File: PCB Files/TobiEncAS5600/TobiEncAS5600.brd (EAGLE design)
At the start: 16 x 16 mm, 4 parts

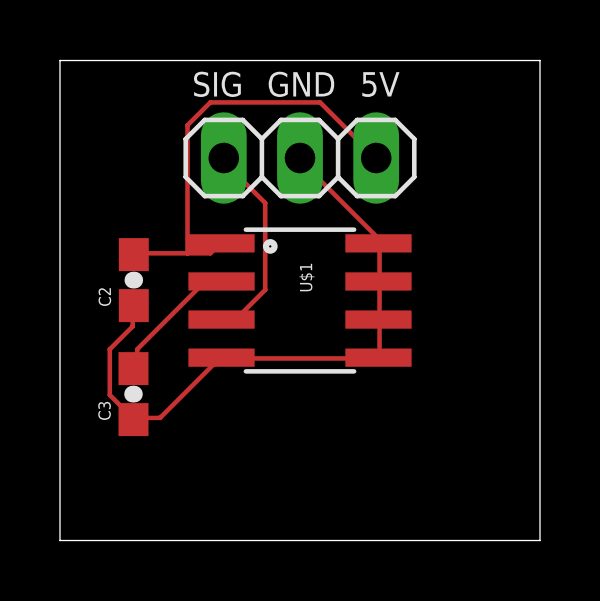
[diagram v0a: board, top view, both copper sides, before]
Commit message: heavier traces on encoder board since it can accomodate them
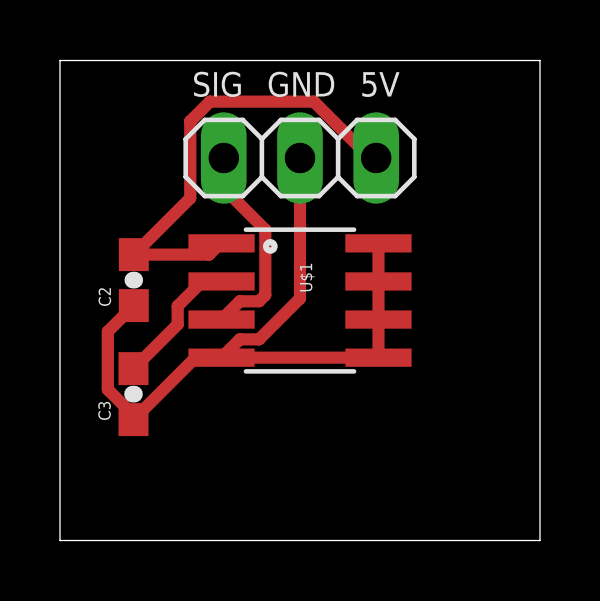
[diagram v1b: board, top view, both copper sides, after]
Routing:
- net GND: track 21.3 -> 25.5 mm
- net 5V: track 14.7 -> 15.7 mm
- net VDD3V3: track 4.51 -> 5.38 mm
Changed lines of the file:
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@@
 <contactref element="C2" pad="2"/>
 <contactref element="JP1" pad="1"/>
-<wire x1="23.0124" y1="93.5736" x2="22.2504" y2="93.5736" width="0.1524" layer="1"/>
-<wire x1="22.2504" y1="93.5736" x2="20.574" y2="93.5736" width="0.1524" layer="1"/>
-<wire x1="23.3172" y1="93.8784" x2="23.0124" y2="93.5736" width="0.1524" layer="1"/>
 <wire x1="20.574" y1="93.5736" x2="20.46" y2="93.53" width="0.1524" layer="1"/>
 <wire x1="23.3172" y1="93.8784" x2="23.3838" y2="93.905" width="0.1524" layer="1"/>
-<wire x1="22.2504" y1="97.8408" x2="22.2504" y2="93.5736" width="0.1524" layer="1"/>
-<wire x1="23.0124" y1="98.6028" x2="22.2504" y2="97.8408" width="0.1524" layer="1"/>
-<wire x1="26.67" y1="98.6028" x2="23.0124" y2="98.6028" width="0.1524" layer="1"/>
-<wire x1="28.4988" y1="96.774" x2="26.67" y2="98.6028" width="0.1524" layer="1"/>
-<wire x1="28.4988" y1="96.774" x2="28.54" y2="96.75" width="0.1524" layer="1"/>
+<wire x1="20.46" y1="93.53" x2="22.9688" y2="93.53" width="0.4064" layer="1"/>
+<wire x1="22.9688" y1="93.53" x2="23.3172" y2="93.8784" width="0.4064" layer="1"/>
+<wire x1="22.99706875" y1="98.6296" x2="22.3424" y2="97.97493125" width="0.4064" layer="1"/>
+<wire x1="28.54" y1="96.75" x2="28.34253125" y2="96.75" width="0.4064" layer="1"/>
+<wire x1="22.3424" y1="95.4124" x2="20.46" y2="93.53" width="0.4064" layer="1"/>
+<wire x1="28.34253125" y1="96.75" x2="26.46293125" y2="98.6296" width="0.4064" layer="1"/>
+<wire x1="22.3424" y1="97.97493125" x2="22.3424" y2="95.4124" width="0.4064" layer="1"/>
+<wire x1="26.46293125" y1="98.6296" x2="22.99706875" y2="98.6296" width="0.4064" layer="1"/>
 </signal>
 <signal name="SIG">
 <contactref element="U$1" pad="3"/>
 <contactref element="JP1" pad="3"/>
-<wire x1="23.9268" y1="91.44" x2="23.4696" y2="91.44" width="0.1524" layer="1"/>
-<wire x1="24.8412" y1="92.3544" x2="23.9268" y2="91.44" width="0.1524" layer="1"/>
-<wire x1="24.8412" y1="95.25" x2="24.8412" y2="92.3544" width="0.1524" layer="1"/>
-<wire x1="23.4696" y1="96.6216" x2="24.8412" y2="95.25" width="0.1524" layer="1"/>
-<wire x1="23.4696" y1="91.44" x2="23.3838" y2="91.365" width="0.1524" layer="1"/>
-<wire x1="23.4696" y1="96.6216" x2="23.46" y2="96.75" width="0.1524" layer="1"/>
+<wire x1="24.63599375" y1="91.9746" x2="24.8443" y2="92.18290625" width="0.4064" layer="1"/>
+<wire x1="23.9934" y1="91.9746" x2="24.63599375" y2="91.9746" width="0.4064" layer="1"/>
+<wire x1="23.46" y1="95.74139375" x2="23.46" y2="96.75" width="0.4064" layer="1"/>
+<wire x1="23.3838" y1="91.365" x2="23.9934" y2="91.9746" width="0.4064" layer="1"/>
+<wire x1="24.8443" y1="92.18290625" x2="24.8443" y2="94.35709375" width="0.4064" layer="1"/>
+<wire x1="24.8443" y1="94.35709375" x2="23.46" y2="95.74139375" width="0.4064" layer="1"/>
 </signal>
 <signal name="GND">
@@
 <contactref element="U$1" pad="7"/>
 <contactref element="U$1" pad="6"/>
-<wire x1="21.336" y1="88.0872" x2="20.574" y2="88.0872" width="0.1524" layer="1"/>
-<wire x1="23.3172" y1="90.0684" x2="21.336" y2="88.0872" width="0.1524" layer="1"/>
-<wire x1="20.574" y1="88.0872" x2="20.45" y2="88.03" width="0.1524" layer="1"/>
-<wire x1="23.3172" y1="90.0684" x2="23.3838" y2="90.095" width="0.1524" layer="1"/>
-<wire x1="20.4216" y1="91.1352" x2="20.4216" y2="91.7448" width="0.1524" layer="1"/>
-<wire x1="19.6596" y1="90.3732" x2="20.4216" y2="91.1352" width="0.1524" layer="1"/>
-<wire x1="19.6596" y1="88.8492" x2="19.6596" y2="90.3732" width="0.1524" layer="1"/>
-<wire x1="20.4216" y1="88.0872" x2="19.6596" y2="88.8492" width="0.1524" layer="1"/>
-<wire x1="20.4216" y1="91.7448" x2="20.46" y2="91.83" width="0.1524" layer="1"/>
-<wire x1="20.4216" y1="88.0872" x2="20.45" y2="88.03" width="0.1524" layer="1"/>
-<wire x1="28.6512" y1="91.2876" x2="28.6512" y2="90.2208" width="0.1524" layer="1"/>
-<wire x1="28.6512" y1="90.2208" x2="28.6162" y2="90.095" width="0.1524" layer="1"/>
-<wire x1="28.6512" y1="91.2876" x2="28.6162" y2="91.365" width="0.1524" layer="1"/>
-<wire x1="28.6512" y1="91.44" x2="28.6512" y2="92.5068" width="0.1524" layer="1"/>
-<wire x1="28.6512" y1="92.5068" x2="28.6162" y2="92.635" width="0.1524" layer="1"/>
-<wire x1="28.6512" y1="91.44" x2="28.6162" y2="91.365" width="0.1524" layer="1"/>
-<wire x1="28.6512" y1="92.6592" x2="28.6512" y2="93.8784" width="0.1524" layer="1"/>
-<wire x1="28.6512" y1="93.8784" x2="28.6162" y2="93.905" width="0.1524" layer="1"/>
-<wire x1="28.6512" y1="92.6592" x2="28.6162" y2="92.635" width="0.1524" layer="1"/>
-<wire x1="28.6512" y1="94.0308" x2="26.0604" y2="96.6216" width="0.1524" layer="1"/>
-<wire x1="26.0604" y1="96.6216" x2="26" y2="96.75" width="0.1524" layer="1"/>
-<wire x1="28.6512" y1="94.0308" x2="28.6162" y2="93.905" width="0.1524" layer="1"/>
-<wire x1="28.4988" y1="90.0684" x2="23.4696" y2="90.0684" width="0.1524" layer="1"/>
-<wire x1="23.4696" y1="90.0684" x2="23.3838" y2="90.095" width="0.1524" layer="1"/>
-<wire x1="28.4988" y1="90.0684" x2="28.6162" y2="90.095" width="0.1524" layer="1"/>
+<wire x1="23.3838" y1="90.095" x2="23.9934" y2="90.7046" width="0.4064" layer="1"/>
+<wire x1="23.9934" y1="90.7046" x2="24.63599375" y2="90.7046" width="0.4064" layer="1"/>
+<wire x1="24.63599375" y1="90.7046" x2="26" y2="92.06860625" width="0.4064" layer="1"/>
+<wire x1="26" y1="92.06860625" x2="26" y2="96.75" width="0.4064" layer="1"/>
+<wire x1="23.3838" y1="90.095" x2="28.6162" y2="90.095" width="0.4064" layer="1"/>
+<wire x1="28.6162" y1="90.095" x2="28.6162" y2="91.365" width="0.4064" layer="1"/>
+<wire x1="28.6162" y1="91.365" x2="28.6162" y2="92.635" width="0.4064" layer="1"/>
+<wire x1="28.6162" y1="92.635" x2="28.6162" y2="93.905" width="0.4064" layer="1"/>
+<wire x1="20.45" y1="88.03" x2="22.515" y2="90.095" width="0.4064" layer="1"/>
+<wire x1="22.515" y1="90.095" x2="23.3838" y2="90.095" width="0.4064" layer="1"/>
+<wire x1="20.45" y1="88.17710625" x2="20.45" y2="88.03" width="0.4064" layer="1"/>
+<wire x1="19.5944" y1="89.03270625" x2="20.45" y2="88.17710625" width="0.4064" layer="1"/>
+<wire x1="20.46" y1="91.83" x2="19.5944" y2="90.9644" width="0.4064" layer="1"/>
+<wire x1="19.5944" y1="90.9644" x2="19.5944" y2="89.03270625" width="0.4064" layer="1"/>
 </signal>
 <signal name="VDD3V3">
 <contactref element="C3" pad="2"/>
 <contactref element="U$1" pad="2"/>
-<wire x1="20.574" y1="90.3732" x2="20.574" y2="89.7636" width="0.1524" layer="1"/>
-<wire x1="22.7076" y1="92.5068" x2="20.574" y2="90.3732" width="0.1524" layer="1"/>
-<wire x1="23.3172" y1="92.5068" x2="22.7076" y2="92.5068" width="0.1524" layer="1"/>
+<wire x1="22.7076" y1="92.5068" x2="23.3172" y2="92.5068" width="0.1524" layer="1"/>
 <wire x1="20.574" y1="89.7636" x2="20.45" y2="89.73" width="0.1524" layer="1"/>
 <wire x1="23.3172" y1="92.5068" x2="23.3838" y2="92.635" width="0.1524" layer="1"/>
+<wire x1="20.45" y1="89.73" x2="21.9233" y2="91.2033" width="0.4064" layer="1"/>
+<wire x1="21.9233" y1="91.2033" x2="21.9233" y2="91.81709375" width="0.4064" layer="1"/>
+<wire x1="21.9233" y1="91.81709375" x2="22.74120625" y2="92.635" width="0.4064" layer="1"/>
+<wire x1="22.74120625" y1="92.635" x2="23.3838" y2="92.635" width="0.4064" layer="1"/>
 </signal>
 </signals>
